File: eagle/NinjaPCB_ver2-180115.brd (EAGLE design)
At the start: 73 x 73 mm, 55 parts, among them IC3 ANALOGSW_AD_SOT23-6NC, IC4 ANALOGSW_TI-SC70-5/6NC, IC6 NAU7802NC, J1 PELTIER, J2 ATX24, J3 HEATER, J4 HEATER_TEMP, Q1 S9013, Q2 IRF520NPBF, Q3 IRF520NPBF, Q4 S9013, Q5 IRF520NPBF, Q6 S9013, Q7 S9013, Q8 S9013, U1 CJT1117-3.3-SOT223

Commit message: finished
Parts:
- removed IC4: ANALOGSW_TI-SC70-5/6NC, PCR-IC:SC70-6NC
- removed J1: PELTIER, Seeed-Connector:H2-3.5-7.0X7.0MM
- removed WELLEXT1, WELLEXT2: (no value), pinhead:1X02
- added JACK: 2.1MMJACKTHM, adafruit:PJ-102A
- added PEL_BLK, PEL_RED: (no value), pinhead:1X01LONG
- added PWR: (no value), pinhead:1X02
- added RELAY: NEC-RELAY2ET2, PCR-Switch:NEC-ET2-N8
- IC3: value ANALOGSW_AD_SOT23-6NC -> ANALOGSW_AD_SOT23-6; device PCR-IC:SOT-23-6NC -> PCR-IC:SOT-23-6
- IC6: value NAU7802NC -> NAU7802; device PCR-IC:SOP-16NC -> PCR-IC:SOP-16
- RD1, RD2, RH1, RH2, RL: device PCR-RCL:R0603NC -> PCR-RCL:R0603
- U$1: value 2.1MMJACKTHM -> (none); device adafruit:PJ-102A -> PCR-Logo:TORI_0.25
- U$2: value NEC-RELAY2ET2 -> (none); device PCR-Switch:NEC-ET2-N8 -> PCR-Logo:TORI_0.25
- moved U$2 73.0 mm to (65.3, 0.43), flipped to the bottom, turned to 0 degrees
- moved U$1 67.1 mm to (5.18, 0.38), turned to 0 degrees
- moved SERIAL 64.5 mm to (66.9, 72.1), flipped to the bottom, turned to 90 degrees
- moved R7 52.1 mm to (55.9, 65.5), turned to 90 degrees
- moved C7 36.7 mm to (54.8, 15.5), turned to 180 degrees
- moved C2 36.1 mm to (65.3, 21.1), turned to 180 degrees
- moved U1 35.8 mm to (65.3, 13.6)
- moved R12 34.0 mm to (63.7, 34.1), turned to 90 degrees
- moved R10 33.9 mm to (31.1, 76.7), turned to 0 degrees
- moved R9 33.2 mm to (51.8, 34.1), turned to 270 degrees
- moved RD1 32.1 mm to (47.2, 76.5)
- moved RD2 32.1 mm to (49.7, 76.5)
- moved R17 31.7 mm to (36.8, 49.8), turned to 90 degrees
- moved Q4 31.6 mm to (33.3, 48.9), turned to 90 degrees
- moved R14 31.3 mm to (29.2, 76.7), turned to 0 degrees
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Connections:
- removed net N$26: WELLEXT1.1, WELLEXT2.1
- removed net N$28: WELLEXT1.2, WELLEXT2.2
- removed net PEL_INA: ESP1.6, ESP2.P$4
- removed net PEL_INB: ESP1.18, ESP2.P$8, IO0.1, IO0.4, R4.2
- new net PWR: PWR.1, SERIAL.4
- net 12V: now also JACK.TIP, RELAY.P$2, RELAY.P$4, RELAY.P$6; no longer U$1.TIP, U$2.P$2, U$2.P$4, U$2.P$6
- net 3V3: now also J4.1, PWR.2; no longer IC4.P$1, IC4.P$6, J4.2
- net GND: now also JACK.RING, JACK.RING_SW; no longer IC4.P$3, U$1.RING, U$1.RING_SW
- net HIGH_TEMP: no longer IC4.P$4
- net N$1: now also J4.2; no longer J4.1
- net N$27: no longer IC4.P$2
- net N$3: now also RELAY.P$5; no longer U$2.P$5
- net N$33: now also RELAY.P$3; no longer U$2.P$3
- net N$36: now also RELAY.P$7; no longer U$2.P$7
- net N$6: now also PEL_RED.1, RELAY.P$8; no longer J1.1, U$2.P$8
- net N$7: now also PEL_BLK.1, RELAY.P$1; no longer J1.2, U$2.P$1
- net PEL_SWA: now also ESP1.6, ESP2.P$4
- net PEL_SWB: now also ESP1.18, ESP2.P$8, IO0.1, IO0.4, R4.2
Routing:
- net GND: track 82.4 -> 528.5 mm, vias 0 -> 42
- net 3V3: track 0.00 -> 171.4 mm
- net 12V: track 112.4 -> 258.7 mm
- net N$3: track 36.5 -> 136.7 mm, vias 0 -> 4
- net PEL_SWB: track 0.00 -> 67.4 mm, vias 0 -> 2
- net PEL_SWA: track 0.00 -> 66.5 mm, vias 0 -> 2
- net HIGH_TEMP: track 0.00 -> 60.8 mm, vias 0 -> 2
- net N$25: track 0.00 -> 59.7 mm
- net N$29: track 0.00 -> 53.2 mm
- net RXD: track 0.00 -> 51.1 mm, vias 0 -> 1
- net HEATER: track 0.00 -> 51.1 mm, vias 0 -> 3
- net TXD: track 0.00 -> 48.5 mm, vias 0 -> 1
- net RESET: track 0.00 -> 43.9 mm
- net FAN: track 0.00 -> 42.8 mm, vias 0 -> 2
- net DRDY: track 0.00 -> 41.6 mm, vias 0 -> 3
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- added copper zone on layer 1, net GND
- added copper zone on layer 16, net GND
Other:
- board size 73 x 73 mm -> 70 x 86 mm
- board text added: "FAN"
- board text added: "GND"
- board text added: "HEATER"
- board text added: "HEATER TEMP"
- board text added: "JACK"
- board text added: "NinjaPCB ver2-180115"
- board text added: "PEL BLK"
- board text added: "PEL RED"
- board text added: "PWR"
- board text added: "RELAY"
- board text added: "RX"
- board text added: "TX"
- board text added: "WELL TEMP"

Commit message: to be ordered
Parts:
- removed R10: 3K, Seeed-Resistor:R0603
- moved U$1 9.04 mm to (14.2, 0.23)
- moved U$2 6.66 mm to (58.6, 0.23)
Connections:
- removed net N$1: J4.2, R10.2
- net HEATER_TEMP: now also J4.2; no longer R10.1
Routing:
- net HEATER_TEMP: track 33.3 -> 50.4 mm
- net N$1: track 16.3 -> 0.00 mm
- net GND: track 528.5 -> 530.4 mm
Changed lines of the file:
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@@
 <text x="20.0406" y="56.1848" size="1.27" layer="21" font="vector" ratio="11">RELAY</text>
 <text x="65.2018" y="72.6186" size="1.27" layer="22" ratio="11" rot="MR0">PWR</text>
-<text x="13.2842" y="2.9972" size="2.286" layer="21" ratio="11">NinjaPCB ver2-180115</text>
-<text x="57.1754" y="3.048" size="2.286" layer="22" ratio="11" rot="MR0">NinjaPCB ver2-180115</text>
+<text x="22.3266" y="2.8448" size="2.286" layer="21" ratio="11">NinjaPCB ver2-180115</text>
+<text x="50.5206" y="2.8448" size="2.286" layer="22" ratio="11" rot="MR0">NinjaPCB ver2-180115</text>
 </plain>
 <attributes>
@@
 <attribute name="NAME" x="60.0964" y="75.6054" size="0.635" layer="33" ratio="10" rot="R270"/>
 </element>
-<element name="R10" library="Seeed-Resistor" package="R0603" value="3K" x="31.115" y="76.6722" smashed="yes">
-<attribute name="MPN" value="RC0603FR-073KL" x="117.475" y="-17.3078" size="1.778" layer="27" display="off"/>
-<attribute name="NAME" x="31.75" y="78.374" size="1.27" layer="25" font="vector" ratio="11" rot="R90"/>
-</element>
 <element name="R14" library="Seeed-Resistor" package="R0603" value="2K" x="29.21" y="76.6722" smashed="yes">
 <attribute name="MPN" value="RC0603FR-072KL" x="120.65" y="-17.3078" size="1.778" layer="27" display="off"/>
@@
 <attribute name="VALUE" x="59.182" y="72.0748" size="1.27" layer="27" rot="R270"/>
 </element>
-<element name="U$1" library="PCR-Logo" package="TORI_0.25" value="" x="5.1816" y="0.381"/>
-<element name="U$2" library="PCR-Logo" package="TORI_0.25" value="" x="65.278" y="0.4318" rot="MR0"/>
+<element name="U$1" library="PCR-Logo" package="TORI_0.25" value="" x="14.224" y="0.2286"/>
+<element name="U$2" library="PCR-Logo" package="TORI_0.25" value="" x="58.6232" y="0.2286" rot="MR0"/>
 </elements>
 <signals>
@@
 <wire x1="28.4884" y1="12.0904" x2="36.4236" y2="12.0904" width="0.2032" layer="16"/>
 <wire x1="38.3066" y1="20.0082" x2="38.4914" y2="20.193" width="0.2032" layer="1"/>
-<wire x1="38.4914" y1="20.193" x2="43.1546" y2="20.193" width="0.2032" layer="1"/>
-<wire x1="43.1546" y1="20.193" x2="43.2816" y2="20.066" width="0.2032" layer="1"/>
-<wire x1="43.2816" y1="20.066" x2="54.483" y2="20.066" width="0.2032" layer="1"/>
 <wire x1="54.483" y1="20.066" x2="54.5592" y2="19.9898" width="0.2032" layer="1"/>
 <wire x1="54.5592" y1="19.9898" x2="55.0926" y2="19.9898" width="0.2032" layer="1"/>
@@
 <wire x1="63.5254" y1="34.6606" x2="62.9666" y2="34.1018" width="0.2032" layer="1"/>
 <wire x1="58.0898" y1="78.4248" x2="66.8528" y2="78.4248" width="0.2032" layer="16"/>
+<wire x1="38.3066" y1="20.066" x2="38.3066" y2="20.0082" width="0.8128" layer="1"/>
+<wire x1="38.3066" y1="20.066" x2="39.9576" y2="21.717" width="1.6256" layer="1"/>
+<wire x1="39.9576" y1="21.717" x2="44.4246" y2="21.717" width="1.6256" layer="1"/>
+<wire x1="44.4246" y1="21.717" x2="45.339" y2="20.8026" width="1.6256" layer="1"/>
+<wire x1="45.339" y1="20.8026" x2="52.2986" y2="20.8026" width="1.6256" layer="1"/>
+<wire x1="52.2986" y1="20.8026" x2="53.093" y2="20.0082" width="1.6256" layer="1"/>
+<wire x1="53.093" y1="20.0082" x2="54.8132" y2="20.0082" width="1.6256" layer="1"/>
 </signal>
 <signal name="3V3">
@@
 <contactref element="IC6" pad="P$5"/>
 <contactref element="R14" pad="1"/>
-<contactref element="R10" pad="1"/>
-<wire x1="29.21" y1="77.4342" x2="31.115" y2="77.4342" width="0.2032" layer="1"/>
 <via x="54.8894" y="75.4784" extent="1-16" drill="0.6"/>
-<wire x1="32.8168" y1="78.4756" x2="32.2072" y2="77.866" width="0.2032" layer="16"/>
-<wire x1="32.2072" y1="77.866" x2="32.2072" y2="77.4342" width="0.2032" layer="16"/>
-<via x="32.2072" y="77.4342" extent="1-16" drill="0.6"/>
-<wire x1="32.2072" y1="77.4342" x2="31.115" y2="77.4342" width="0.2032" layer="1"/>
-<wire x1="50.8762" y1="78.4756" x2="32.8168" y2="78.4756" width="0.2032" layer="16"/>
+<via x="31.4452" y="77.4342" extent="1-16" drill="0.6"/>
+<wire x1="50.8762" y1="78.4756" x2="32.4866" y2="78.4756" width="0.2032" layer="16"/>
 <wire x1="50.8762" y1="78.4756" x2="53.8734" y2="75.4784" width="0.2032" layer="16"/>
 <wire x1="53.8734" y1="75.4784" x2="54.8894" y2="75.4784" width="0.2032" layer="16"/>
@@
 <wire x1="56.5404" y1="72.4304" x2="54.8894" y2="74.0814" width="0.2032" layer="1"/>
 <wire x1="54.8894" y1="74.0814" x2="54.8894" y2="75.4784" width="0.2032" layer="1"/>
+<contactref element="J4" pad="2"/>
+<wire x1="29.6164" y1="66.69" x2="29.6164" y2="74.4116" width="0.2032" layer="1"/>
+<wire x1="35.3314" y1="67.7848" x2="33.2512" y2="67.7848" width="0.2032" layer="1"/>
+<wire x1="33.2512" y1="67.7848" x2="31.8516" y2="66.3852" width="0.2032" layer="1"/>
+<wire x1="31.8516" y1="66.3852" x2="29.9212" y2="66.3852" width="0.2032" layer="1"/>
+<wire x1="29.9212" y1="66.3852" x2="29.6164" y2="66.69" width="0.2032" layer="1"/>
+<wire x1="29.21" y1="77.4342" x2="30.1752" y2="77.4342" width="0.2032" layer="1"/>
+<wire x1="30.1752" y1="77.4342" x2="31.4452" y2="77.4342" width="0.2032" layer="1"/>
+<wire x1="29.6164" y1="74.4116" x2="30.1752" y2="74.9704" width="0.2032" layer="1"/>
+<wire x1="30.1752" y1="74.9704" x2="30.1752" y2="77.4342" width="0.2032" layer="1"/>
+<wire x1="32.4866" y1="78.4756" x2="31.4452" y2="77.4342" width="0.2032" layer="16"/>
 </signal>
 <signal name="N$4">
@@
 <wire x1="24.8412" y1="75.7578" x2="24.8412" y2="71.9732" width="5.08" layer="1"/>
 </signal>
-<signal name="N$1">
-<contactref element="J4" pad="2"/>
-<contactref element="R10" pad="2"/>
-<wire x1="29.6164" y1="66.69" x2="29.6164" y2="74.4116" width="0.2032" layer="1"/>
-<wire x1="29.6164" y1="74.4116" x2="31.115" y2="75.9102" width="0.2032" layer="1"/>
-<wire x1="35.3314" y1="67.7848" x2="33.2512" y2="67.7848" width="0.2032" layer="1"/>
-<wire x1="33.2512" y1="67.7848" x2="31.8516" y2="66.3852" width="0.2032" layer="1"/>
-<wire x1="31.8516" y1="66.3852" x2="29.9212" y2="66.3852" width="0.2032" layer="1"/>
-<wire x1="29.9212" y1="66.3852" x2="29.6164" y2="66.69" width="0.2032" layer="1"/>
-</signal>
 <signal name="PWR">

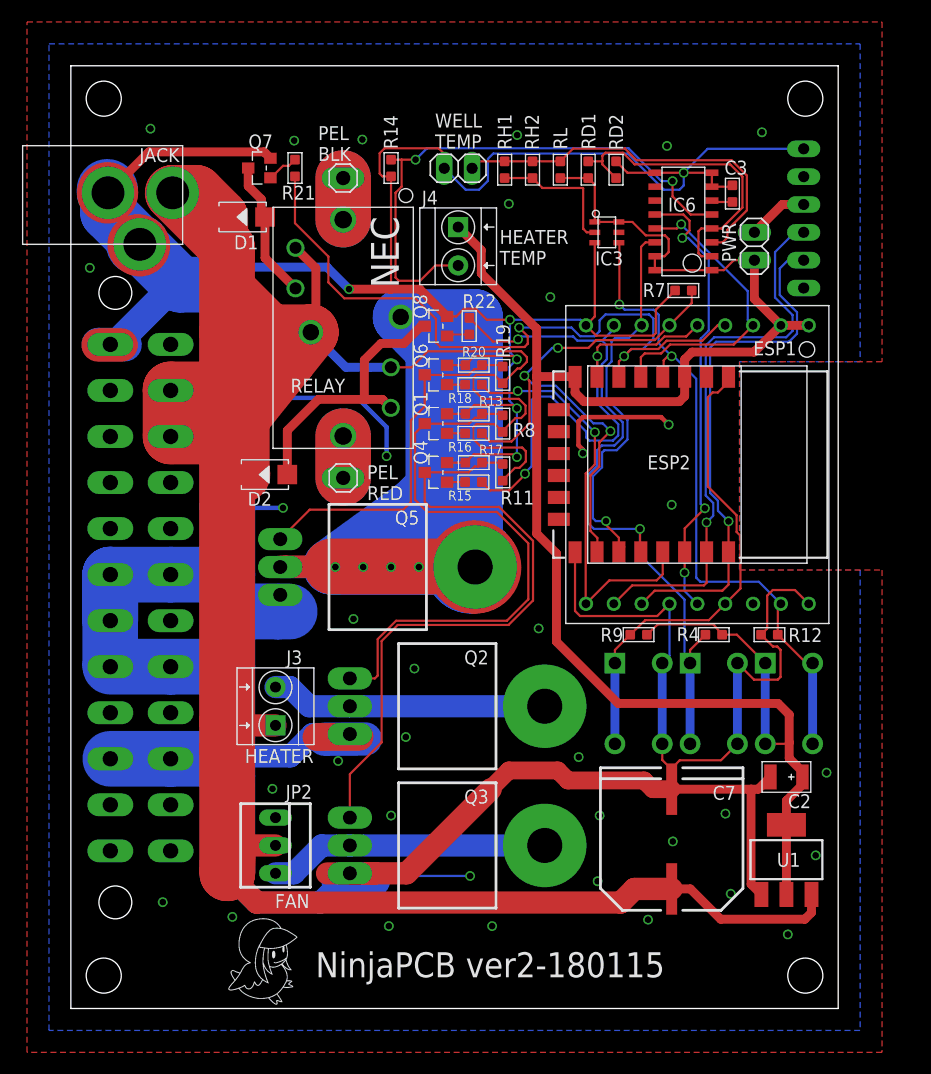
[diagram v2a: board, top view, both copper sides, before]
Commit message: npn to pnp. added pullups and pulldowns
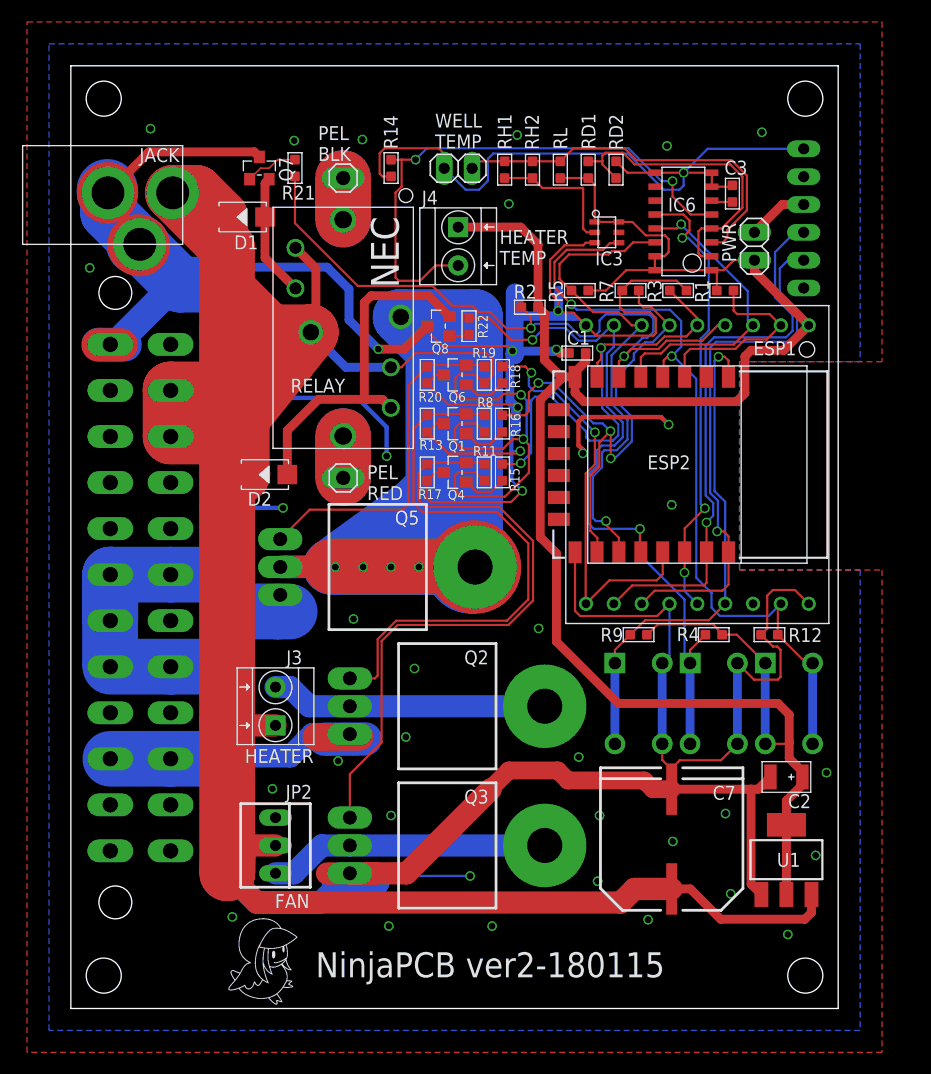
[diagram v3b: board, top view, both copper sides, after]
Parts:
- added C1: 100nf, Seeed-Capacitor:C0603
- added R1, R2, R3, R5: 10K 1/10W, Seeed-Resistor:R0603
- Q1, Q4, Q6, Q7, Q8: value S9013 -> S8550
- moved R7 4.83 mm to (51.1, 65.5)
- moved R13 4.33 mm to (32.5, 53.4), turned to 180 degrees
- moved R17 4.33 mm to (32.5, 48.9), turned to 180 degrees
- moved R20 4.33 mm to (32.5, 57.8), turned to 180 degrees
- moved R15 2.79 mm to (39.4, 48.9), turned to 0 degrees
- moved R16 2.79 mm to (39.4, 53.4), turned to 0 degrees
- moved R18 2.79 mm to (39.4, 57.8), turned to 0 degrees
- moved Q1 1.75 mm to (35.1, 53.4)
- moved Q4 1.75 mm to (35.1, 48.9)
- moved Q6 1.75 mm to (35.1, 57.8)
- moved R11 1.68 mm to (37.7, 48.9)
- moved R19 1.68 mm to (37.7, 57.8)
- moved R8 1.68 mm to (37.7, 53.4)
- moved Q8 0.23 mm to (33.5, 62.2)
- turned Q7 to 0 degrees
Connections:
- new net EN: ESP1.3, ESP2.P$2, R1.1
- net 3V3: now also C1.1, R1.2, R2.1, R5.1; no longer ESP1.3, ESP2.P$2
- net FAN: now also R3.2
- net GND: now also C1.2, Q1.3, Q4.3, Q6.3, Q7.3, Q8.3, R3.1; no longer Q1.2, Q4.2, Q6.2, Q7.2, Q8.2
- net N$25: now also Q4.2; no longer Q4.3
- net N$29: now also Q1.2; no longer Q1.3
- net N$33: now also Q7.2; no longer Q7.3
- net N$36: now also Q8.2; no longer Q8.3
- net N$5: now also Q6.2; no longer Q6.3
- net PEL_SWA: now also R2.2
- net SDIO: now also R5.2
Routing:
- net GND: track 530.4 -> 581.0 mm
- net EN: track 0.00 -> 18.6 mm
- net 3V3: track 171.4 -> 186.3 mm
- net HIGH_TEMP: track 60.8 -> 74.0 mm
- net 12V: track 258.7 -> 270.5 mm, vias 0 -> 2
- net SDIO: track 36.4 -> 46.8 mm
- net N$36: track 25.4 -> 32.7 mm
- net PEL_SWA: track 66.5 -> 62.6 mm
- net RESET: track 43.9 -> 46.4 mm, vias 0 -> 1
- net N$32: track 1.65 -> 4.15 mm
- net N$31: track 1.65 -> 4.10 mm
- net N$30: track 1.65 -> 4.08 mm
- net N$34: track 2.92 -> 4.88 mm
- net HEATER: track 51.1 -> 49.4 mm
- net N$33: track 12.8 -> 11.3 mm
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
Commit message: added hole for gromet #digikey 36-733-ND
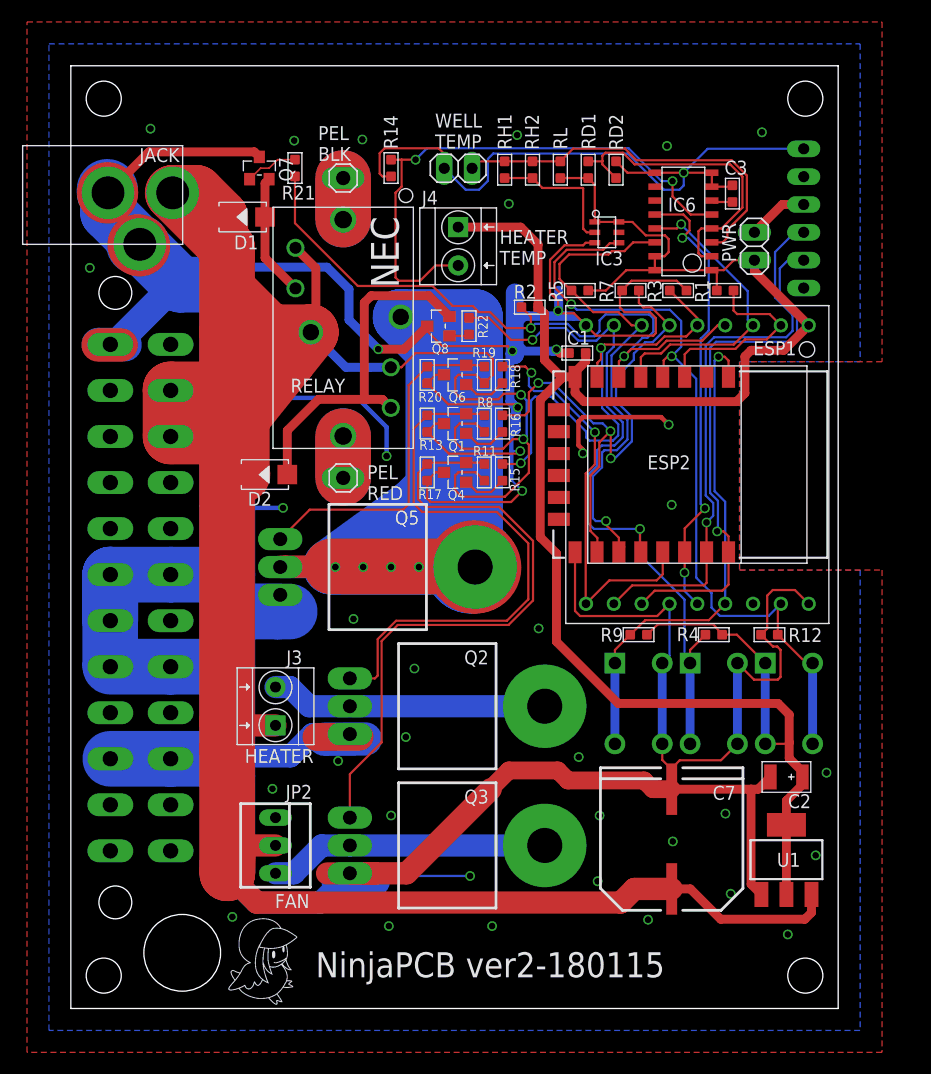
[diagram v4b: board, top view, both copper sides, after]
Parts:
- moved U$2 5.82 mm to (64.4, 0.18)
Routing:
- net GND: track 581.0 -> 584.9 mm
